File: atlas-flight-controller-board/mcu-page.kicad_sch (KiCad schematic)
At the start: 2 parts, among them J4 5V Input Power, U2 DEV-16771

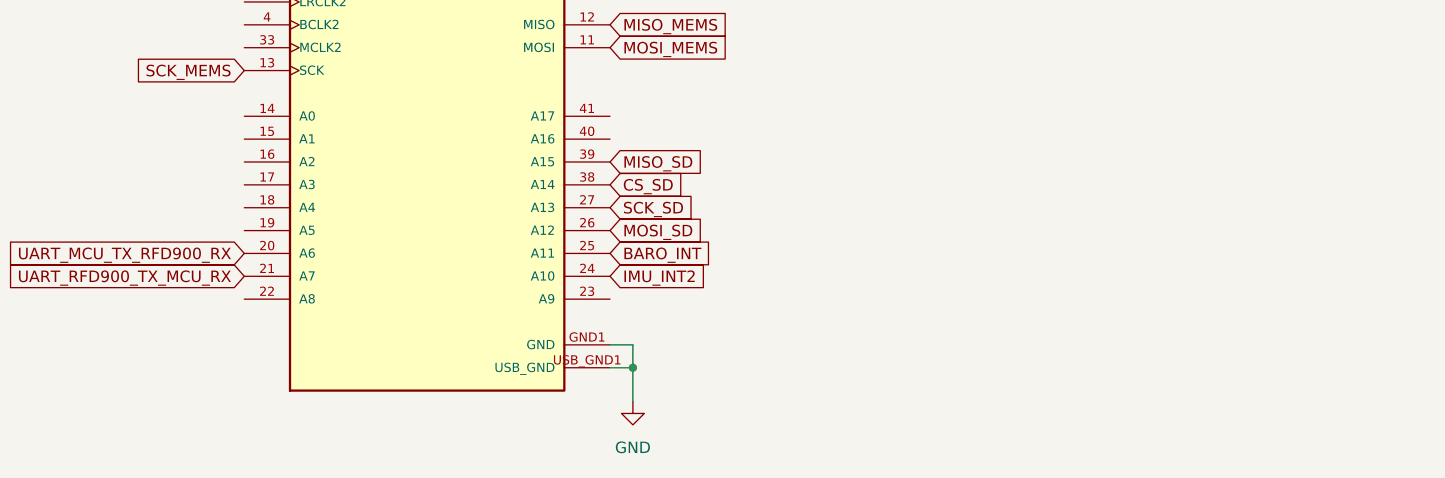
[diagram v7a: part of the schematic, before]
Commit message: Fixing a couple things here and there. Need to add LEDs still and route external LEDs
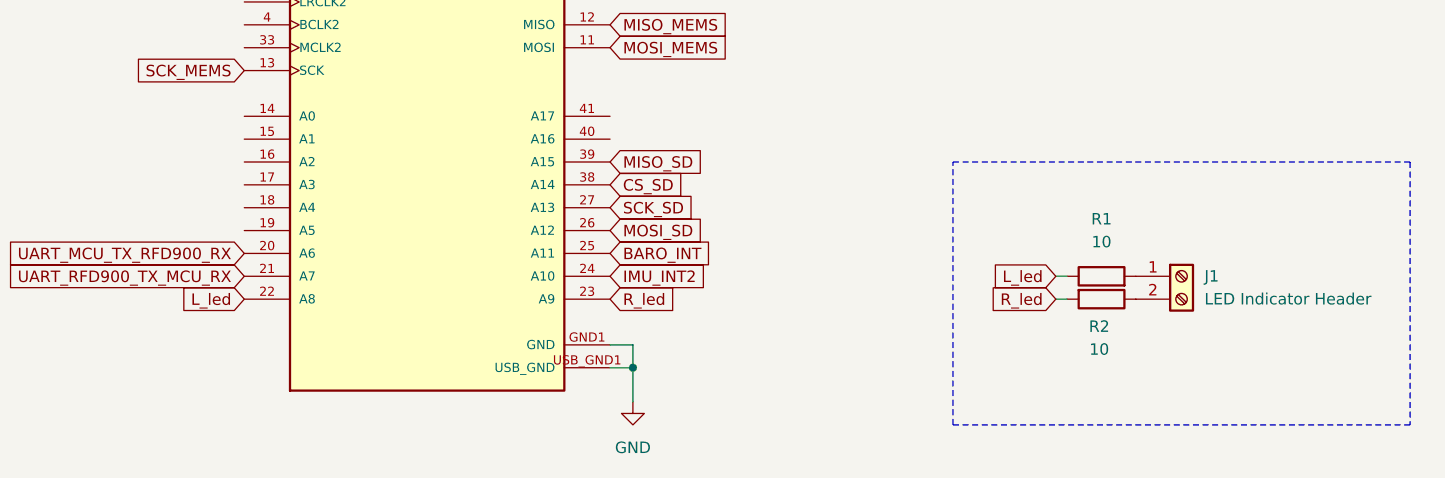
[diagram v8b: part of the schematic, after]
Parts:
- added J1: LED Indicator Header, TerminalBlock:TerminalBlock_Xinya_XY308-2.54-2P_1x02_P2.54mm_Horizontal, symbol Connector:Screw_Terminal_01x02
- added R1, R2: 10, Resistor_SMD:R_0603_1608Metric_Pad0.98x0.95mm_HandSolder, symbol Device:R
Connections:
- net L_led: now reaches U2.22 (A8)
- net L_led: now also R1.1
- net R_led: now reaches U2.23 (A9)
- net R_led: now also R2.2
- new net: J1.1 (Pin_1), R1.2
- new net: J1.2 (Pin_2), R2.1
